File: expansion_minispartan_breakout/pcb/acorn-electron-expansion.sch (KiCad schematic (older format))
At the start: 19 parts, among them P1 Acorn Electron Expansion Conn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, P2 CONN_02X24, P3 5V / 5V0, U1 74hct125d, U2 74LVC245 D0-7, U3 74LVC245 A0-7, U4 74LVC245 A8-15, U5 74LVC245, U6 scarab_mini_spartan_6_lx25

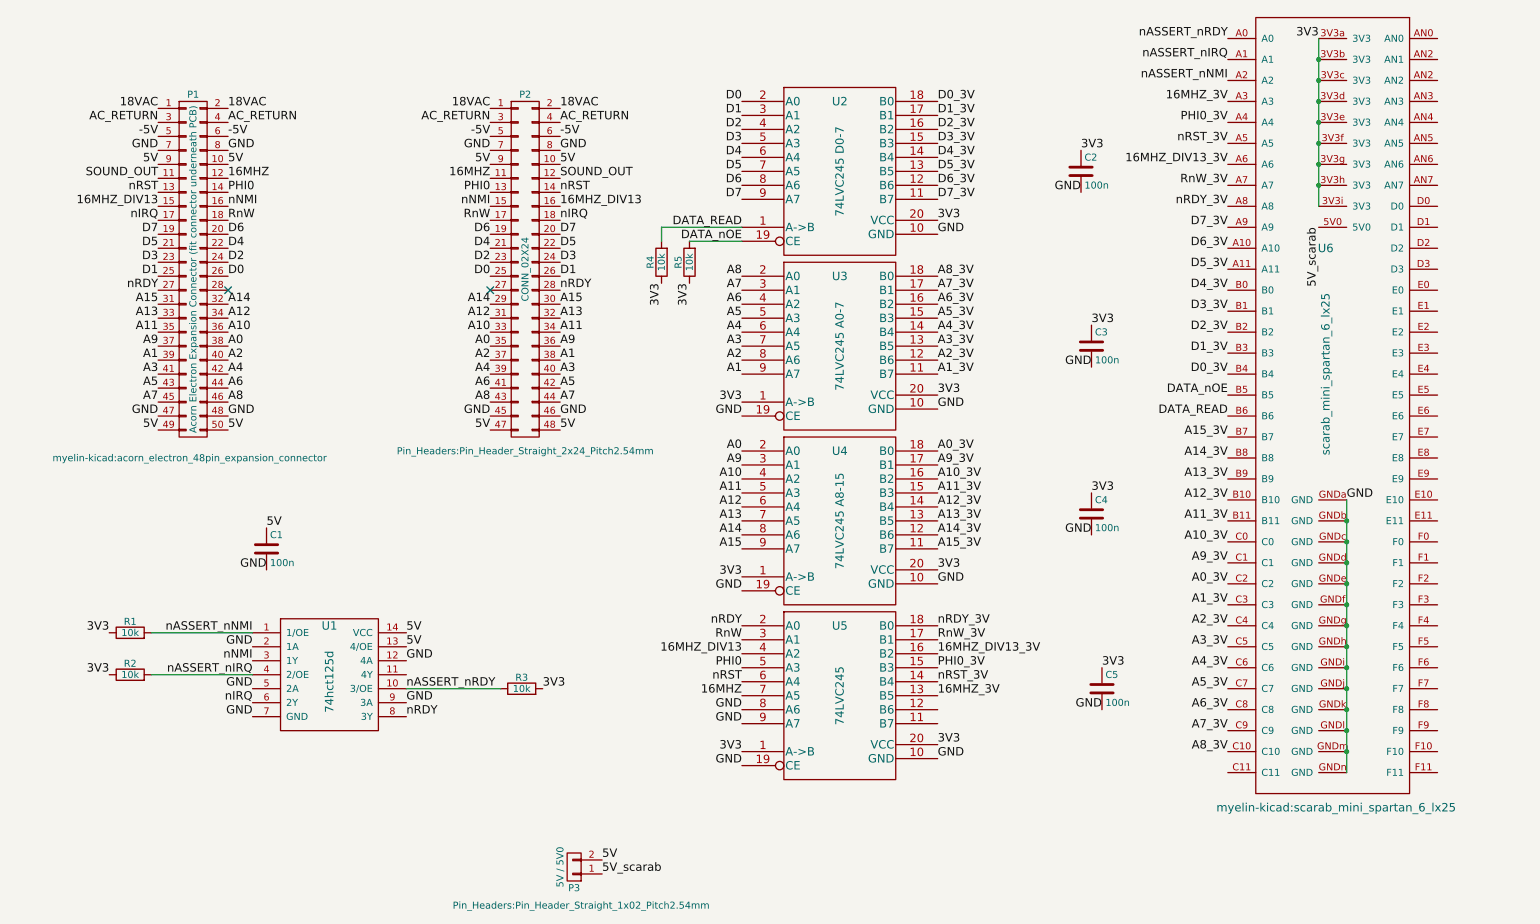
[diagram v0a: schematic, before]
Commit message: Updates to expansion_minispartan_breakout to allow the FPGA to drive the bus
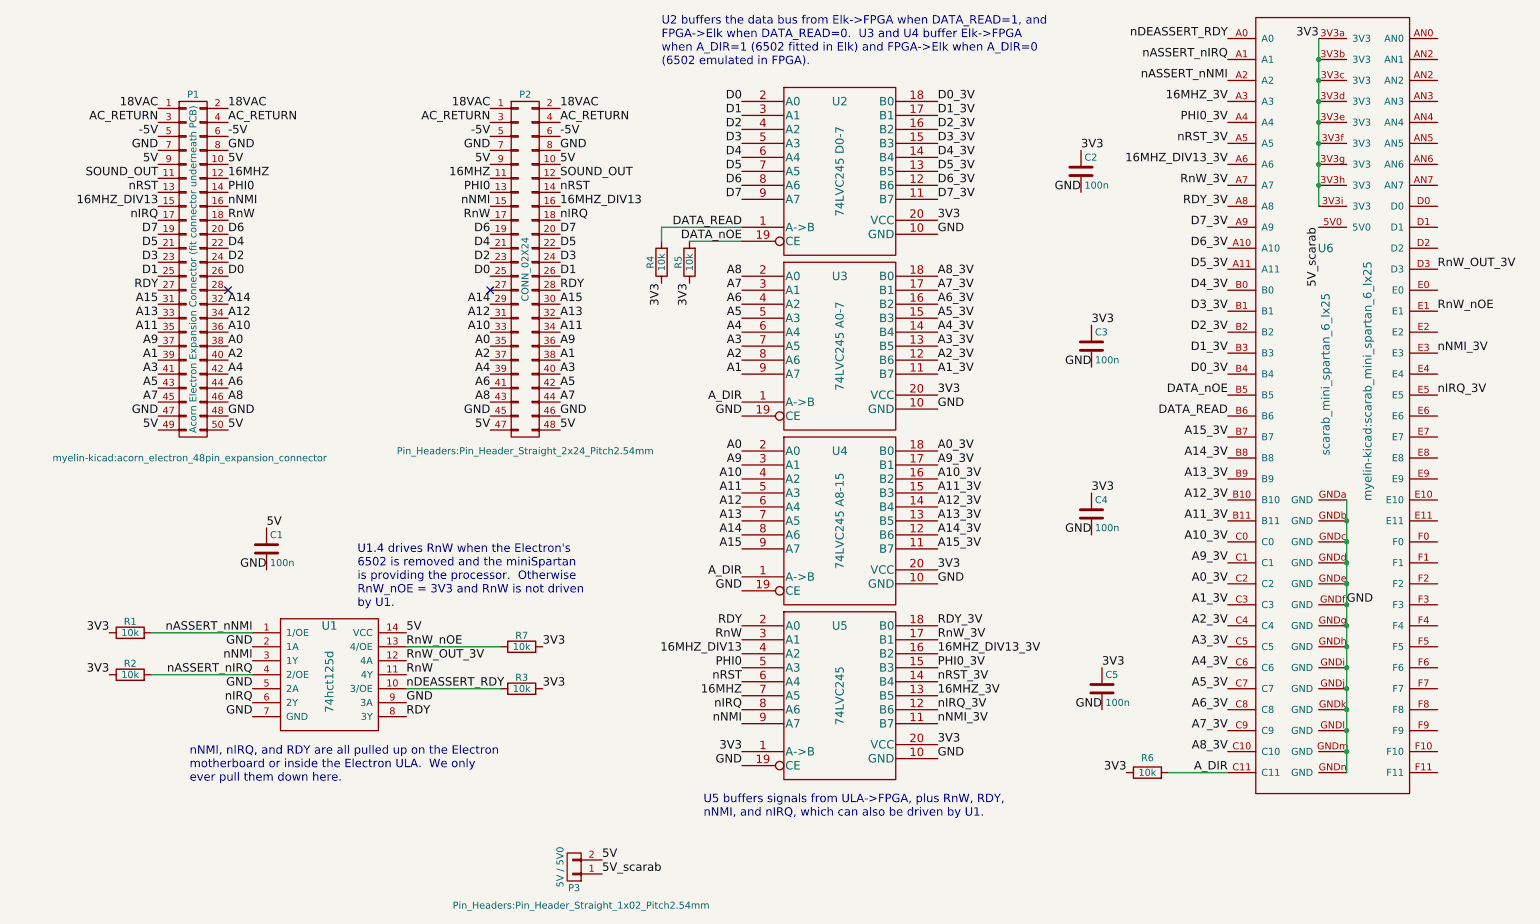
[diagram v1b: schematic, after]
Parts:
- added R6, R7: 10k, Resistors_SMD:R_0805_HandSoldering, symbol R0805
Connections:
- net 3V3: now also R6.1, R7.2; no longer U3.1 (A->B), U4.1 (A->B)
- net 5V: no longer U1.13 (4/OE)
- net GND: no longer U1.12 (4A), U5.8 (A6), U5.9 (A7)
- net RnW: now also U1.11 (4Y)
- net nIRQ: now also U5.8 (A6)
- net nNMI: now also U5.9 (A7)
- net nNMI_3V: now reaches U5.11 (B7)
- net nNMI_3V: now also U6.E3
- net nIRQ_3V: now reaches U5.12 (B6)
- net nIRQ_3V: now also U6.E5
- net A_DIR: now reaches U6.C11
- net A_DIR: now also U3.1 (A->B), U4.1 (A->B), R6.2
- net RnW_OUT_3V: now reaches U6.D3
- net RnW_OUT_3V: now also U1.12 (4A)
- net RnW_nOE: now reaches U6.E1
- net RnW_nOE: now also U1.13 (4/OE), R7.1
- net nASSERT_nRDY renamed nDEASSERT_RDY
- net nRDY renamed RDY
- net nRDY_3V renamed RDY_3V
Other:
- note added: "U1.4 drives RnW when the Electron's\n6502 is removed and the miniSpartan\nis providing the processor. Otherwise\nRnW_nOE = 3V3 and RnW is not driven\nby U1."
- note added: "U2 buffers the data bus from Elk->FPGA when DATA_READ=1, and\nFPGA->Elk when DATA_READ=0. U3 and U4 buffer Elk->FPGA\nwhen A_DIR=1 (6502 fitted in Elk) and FPGA->Elk when A_DIR=0\n(6502 emulated in FPGA)."
- note added: "U5 buffers signals from ULA->FPGA, plus RnW, RDY,\nnNMI, and nIRQ, which can also be driven by U1."
- note added: "nNMI, nIRQ, and RDY are all pulled up on the Electron\nmotherboard or inside the Electron ULA. We only\never pull them down here."
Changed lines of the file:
@@
 LIBS:contrib
 LIBS:valves
+LIBS:scarab_mini_spartan_6_lx25
 LIBS:acorn-electron-expansion-cache
 EELAYER 25 0
@@
 D1
 Text Label 4300 2600 0    60   ~ 0
-nRDY
+RDY
 Text Label 4300 2000 0    60   ~ 0
 16MHZ_DIV13
@@
 nIRQ
 Text Label 3200 5650 0    60   ~ 0
-nRDY
+RDY
 $Comp
 L 74hct125d U1
@@
 GND
 Text Label 3200 5250 0    60   ~ 0
-GND
+RnW_OUT_3V
 Text Label 2100 5150 2    60   ~ 0
 GND
@@
 D1
 Text Label 1425 2600 2    60   ~ 0
-nRDY
+RDY
 Text Label 1425 2000 2    60   ~ 0
 16MHZ_DIV13
@@
 3V3
 Text Label 5600 4650 2    60   ~ 0
-3V3
+A_DIR
 Text Label 5600 3400 2    60   ~ 0
-3V3
+A_DIR
 $Comp
 L R0805 R4
@@
 nASSERT_nNMI
 Text Label 3200 5450 0    60   ~ 0
-nASSERT_nRDY
+nDEASSERT_RDY
 Text Label 2100 5350 2    60   ~ 0
 nASSERT_nIRQ
@@
 3V3
 Text Label 5600 5000 2    60   ~ 0
-nRDY
+RDY
 Text Label 7000 5000 0    60   ~ 0
-nRDY_3V
+RDY_3V
 Text Label 5600 5600 2    60   ~ 0
-GND
+nIRQ
 Text Label 5600 5700 2    60   ~ 0
-GND
+nNMI
 Text Label 3200 5150 0    60   ~ 0
-5V
+RnW_nOE
 $Comp
 L C0805 C1
@@
 F 0 "U6" H 9775 7300 60  0000 C CNN
 F 1 "scarab_mini_spartan_6_lx25" V 9775 6400 60  0000 C CNN
-F 2 "myelin-kicad:scarab_mini_spartan_6_lx25" H 9850 3300 60  0000 C CNN
+F 2 "myelin-kicad:scarab_mini_spartan_6_lx25" V 10075 6350 60  0000 C CNN
 F 3 "" H 8825 4650 60  0000 C CNN
 	1    9775 4800
@@
 Text Label 9725 800  2    60   ~ 0
 3V3
-Text Label 9925 4100 0    60   ~ 0
+Text Label 9925 4850 0    60   ~ 0
 GND
 Wire Wire Line
@@
 5V_scarab
 Text Label 9075 800  2    60   ~ 0
-nASSERT_nRDY
+nDEASSERT_RDY
 Text Label 9075 950  2    60   ~ 0
 nASSERT_nIRQ
@@
 16MHZ_3V
 Text Label 9075 2000 2    60   ~ 0
-nRDY_3V
+RDY_3V
 Text Label 9075 3200 2    60   ~ 0
 D0_3V
@@
 	-1   0    0    1
 $EndComp
+Text Label 9075 6050 2    60   ~ 0
+A_DIR
+$Comp
+L R0805 R6
+U 1 1 59370791
+P 8500 6050
+F 0 "R6" V 8605 6050 50  0000 C CNN
+F 1 "10k" V 8500 6050 50  0000 C CNN
+F 2 "Resistors_SMD:R_0805_HandSoldering" V 8430 6050 50  0001 C CNN
+F 3 "" H 8500 6050 50  0000 C CNN
+	1    8500 6050
+	0    -1   -1   0
+$EndComp
+Text Label 8350 6050 2    60   ~ 0
+3V3
+Wire Wire Line
+	8650 6050 9075 6050
+Text Label 3200 5350 0    60   ~ 0
+RnW
+$Comp
+L R0805 R7
+U 1 1 59371B96
+P 4025 5150
+F 0 "R7" V 4105 5150 50  0000 C CNN
+F 1 "10k" V 4025 5150 50  0000 C CNN
+F 2 "Resistors_SMD:R_0805_HandSoldering" V 3955 5150 50  0001 C CNN
+F 3 "" H 4025 5150 50  0000 C CNN
+	1    4025 5150
+	0    -1   -1   0
+$EndComp
+Text Label 4175 5150 0    60   ~ 0
+3V3
+Text Notes 2850 4875 0    60   ~ 0
+U1.4 drives RnW when the Electron's\n6502 is removed and the miniSpartan\nis providing the processor.  Otherwise\nRnW_nOE = 3V3 and RnW is not driven\nby U1.
+Text Notes 1650 6125 0    60   ~ 0
+nNMI, nIRQ, and RDY are all pulled up on the Electron\nmotherboard or inside the Electron ULA.  We only\never pull them down here.
+Text Notes 5025 1000 0    60   ~ 0
+U2 buffers the data bus from Elk->FPGA when DATA_READ=1, and\nFPGA->Elk when DATA_READ=0.  U3 and U4 buffer Elk->FPGA\nwhen A_DIR=1 (6502 fitted in Elk) and FPGA->Elk when A_DIR=0\n(6502 emulated in FPGA).
+Text Notes 5325 6375 0    60   ~ 0
+U5 buffers signals from ULA->FPGA, plus RnW, RDY,\nnNMI, and nIRQ, which can also be driven by U1.
+Wire Wire Line
+	3875 5150 3200 5150
+Text Label 7000 5600 0    60   ~ 0
+nIRQ_3V
+Text Label 7000 5700 0    60   ~ 0
+nNMI_3V
+Text Label 10575 3350 0    60   ~ 0
+nIRQ_3V
+Text Label 10575 3050 0    60   ~ 0
+nNMI_3V
+Text Label 10575 2750 0    60   ~ 0
+RnW_nOE
+Text Label 10575 2450 0    60   ~ 0
+RnW_OUT_3V
 $EndSCHEMATC
